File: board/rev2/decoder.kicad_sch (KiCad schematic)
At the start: 4 parts, among them U10 74VHC161

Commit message: 3.3V LDO
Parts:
- removed R22, R23: 33, Resistor_SMD:R_0402_1005Metric, symbol Device:R_Small_US
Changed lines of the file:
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@@
+	)
+	(junction
+		(at 173.99 76.2)
+		(diameter 0)
+		(color 0 0 0 0)
 	)
 	(junction
@@
 	)
 	(junction
-		(at 161.29 95.25)
-		(diameter 0)
-		(color 0 0 0 0)
-	)
-	(junction
 		(at 168.91 68.58)
 		(diameter 0)
@@
 		)
 	)
-	(wire
-		(pts
-			(xy 161.29 95.25) (xy 161.29 50.8)
-		)
-		(stroke
-			(width 0)
-			(type default)
-		)
-	)
 	(bus
 		(pts
@@
 	(wire
 		(pts
-			(xy 142.24 95.25) (xy 161.29 95.25)
+			(xy 142.24 76.2) (xy 173.99 76.2)
 		)
 		(stroke
@@
 	(wire
 		(pts
+			(xy 173.99 76.2) (xy 173.99 50.8)
+		)
+		(stroke
+			(width 0)
+			(type default)
+		)
+	)
+	(wire
+		(pts
 			(xy 123.19 71.12) (xy 125.73 71.12)
 		)
@@
 	(wire
 		(pts
-			(xy 161.29 50.8) (xy 171.45 50.8)
+			(xy 173.99 50.8) (xy 180.34 50.8)
 		)
 		(stroke
@@
 	(wire
 		(pts
+			(xy 173.99 76.2) (xy 173.99 106.68)
+		)
+		(stroke
+			(width 0)
+			(type default)
+		)
+	)
+	(wire
+		(pts
 			(xy 91.44 55.88) (xy 91.44 58.42)
 		)
@@
 	(wire
 		(pts
-			(xy 161.29 106.68) (xy 171.45 106.68)
+			(xy 173.99 106.68) (xy 180.34 106.68)
 		)
 		(stroke
@@
 	(wire
 		(pts
-			(xy 161.29 95.25) (xy 161.29 106.68)
-		)
-		(stroke
-			(width 0)
-			(type default)
-		)
-	)
-	(wire
-		(pts
 			(xy 44.45 48.26) (xy 67.31 48.26)
 		)
@@
 	(wire
 		(pts
-			(xy 176.53 50.8) (xy 180.34 50.8)
-		)
-		(stroke
-			(width 0)
-			(type default)
-		)
-	)
-	(wire
-		(pts
 			(xy 67.31 48.26) (xy 163.83 48.26)
 		)
@@
 		(pts
 			(xy 168.91 124.46) (xy 180.34 124.46)
-		)
-		(stroke
-			(width 0)
-			(type default)
-		)
-	)
-	(wire
-		(pts
-			(xy 176.53 106.68) (xy 180.34 106.68)
 		)
 		(stroke
@@
 	(hierarchical_label "RGB_CLK"
 		(shape input)
-		(at 142.24 95.25 180)
+		(at 142.24 76.2 180)
 		(effects
 			(font
@@
 	)
 	(symbol
-		(lib_id "Device:R_Small_US")
-		(at 173.99 50.8 90)
-		(unit 1)
-		(exclude_from_sim no)
-		(in_bom yes)
-		(on_board yes)
-		(dnp no)
-		(property "Reference" "R22"
-			(at 173.99 53.086 90)
-			(effects
-				(font
-					(size 1.27 1.27)
-				)
-			)
-		)
-		(property "Value" "33"
-			(at 173.99 55.118 90)
-			(effects
-				(font
-					(size 1.27 1.27)
-				)
-			)
-		)
-		(property "Footprint" "Resistor_SMD:R_0402_1005Metric"
-			(at 173.99 50.8 0)
-			(effects
-				(font
-					(size 1.27 1.27)
-				)
-				(hide yes)
-			)
-		)
-		(property "Datasheet" "~"
-			(at 173.99 50.8 0)
-			(effects
-				(font
-					(size 1.27 1.27)
-				)
-				(hide yes)
-			)
-		)
-		(property "Description" "Resistor, small US symbol"
-			(at 173.99 50.8 0)
-			(effects
-				(font
-					(size 1.27 1.27)
-				)
-				(hide yes)
-			)
-		)
-		(property "Part" "0402WGF330JTCE"
-			(at 173.99 50.8 90)
-			(effects
-				(font
-					(size 1.27 1.27)
-				)
-				(hide yes)
-			)
-		)
-		(property "LCSC" "C25105"
-			(at 173.99 50.8 90)
-			(effects
-				(font
-					(size 1.27 1.27)
-				)
-				(hide yes)
-			)
-		)
-		(pin "2"
-		)
-		(pin "1"
-		)
-		(instances
-			(project "mainboard"
-				(path "/32eb05c7-b4a6-42f3-8fb3-43453631100f/2c9586de-ca2f-4a0b-8ff8-8fdad1d1abcc"
-					(reference "R22")
-					(unit 1)
-				)
-			)
-		)
-	)
-	(symbol
 		(lib_id "Device:C_Small")
 		(at 99.06 58.42 90)
@@
 					(unit 1)
 				)
-			)
-		)
-	)
-	(symbol
-		(lib_id "Device:R_Small_US")
-		(at 173.99 106.68 90)
-		(unit 1)
-		(exclude_from_sim no)
-		(in_bom yes)
-		(on_board yes)
-		(dnp no)
-		(property "Reference" "R23"
-			(at 173.99 108.966 90)
-			(effects
-				(font
-					(size 1.27 1.27)
-				)
-			)
-		)
-		(property "Value" "33"
-			(at 173.99 110.998 90)
-			(effects
-				(font
-					(size 1.27 1.27)
-				)
-			)
-		)
-		(property "Footprint" "Resistor_SMD:R_0402_1005Metric"
-			(at 173.99 106.68 0)
-			(effects
-				(font
-					(size 1.27 1.27)
-				)
-				(hide yes)
-			)
-		)
-		(property "Datasheet" "~"
-			(at 173.99 106.68 0)
-			(effects
-				(font
-					(size 1.27 1.27)
-				)
-				(hide yes)
-			)
-		)
-		(property "Description" "Resistor, small US symbol"
-			(at 173.99 106.68 0)
-			(effects
-				(font
-					(size 1.27 1.27)
-				)
-				(hide yes)
-			)
-		)
-		(property "Part" "0402WGF330JTCE"
-			(at 173.99 106.68 90)
-			(effects
-				(font
-					(size 1.27 1.27)
-				)
-				(hide yes)
-			)
-		)
-		(property "LCSC" "C25105"
-			(at 173.99 106.68 90)
-			(effects
-				(font
-					(size 1.27 1.27)
-				)
-				(hide yes)
-			)
-		)
-		(pin "2"
-		)
-		(pin "1"
-		)
-		(instances
-			(project ""
-				(path "/32eb05c7-b4a6-42f3-8fb3-43453631100f/2c9586de-ca2f-4a0b-8ff8-8fdad1d1abcc"
-					(reference "R23")
-					(unit 1)
-				)

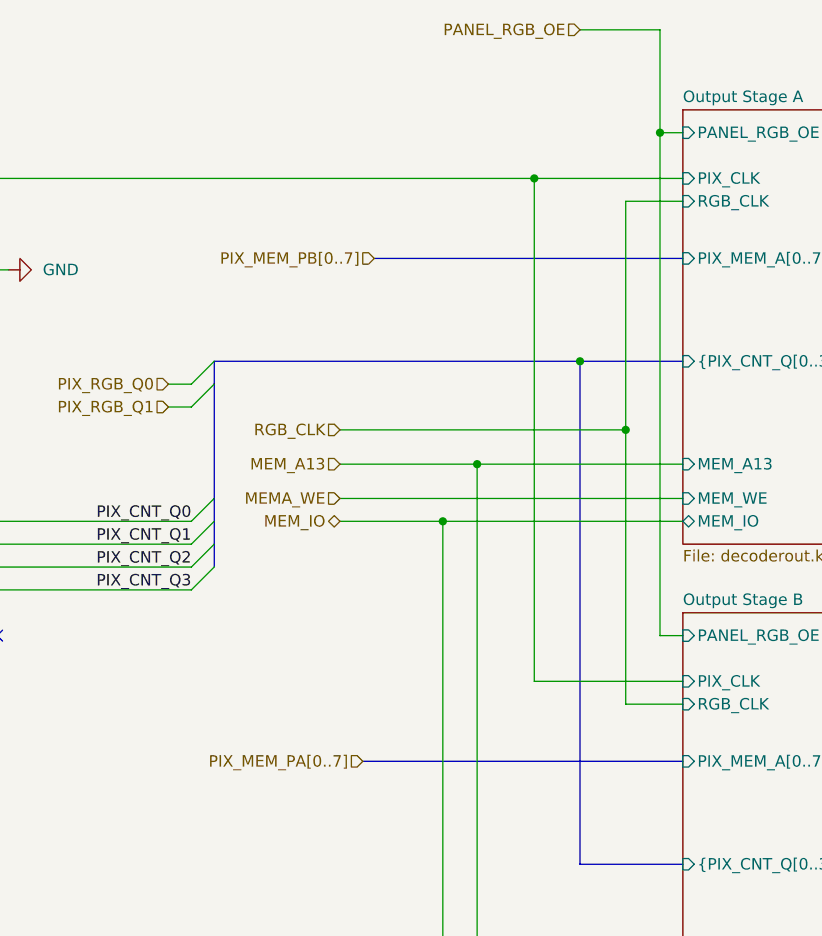
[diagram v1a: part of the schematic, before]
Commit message: Rough full board layout
also, start re-organizing which pins of buffers/gates are used for what

still need to reorder the mem i/o lines to align better

also fix duplicate pullups and fix mem_io isolation res
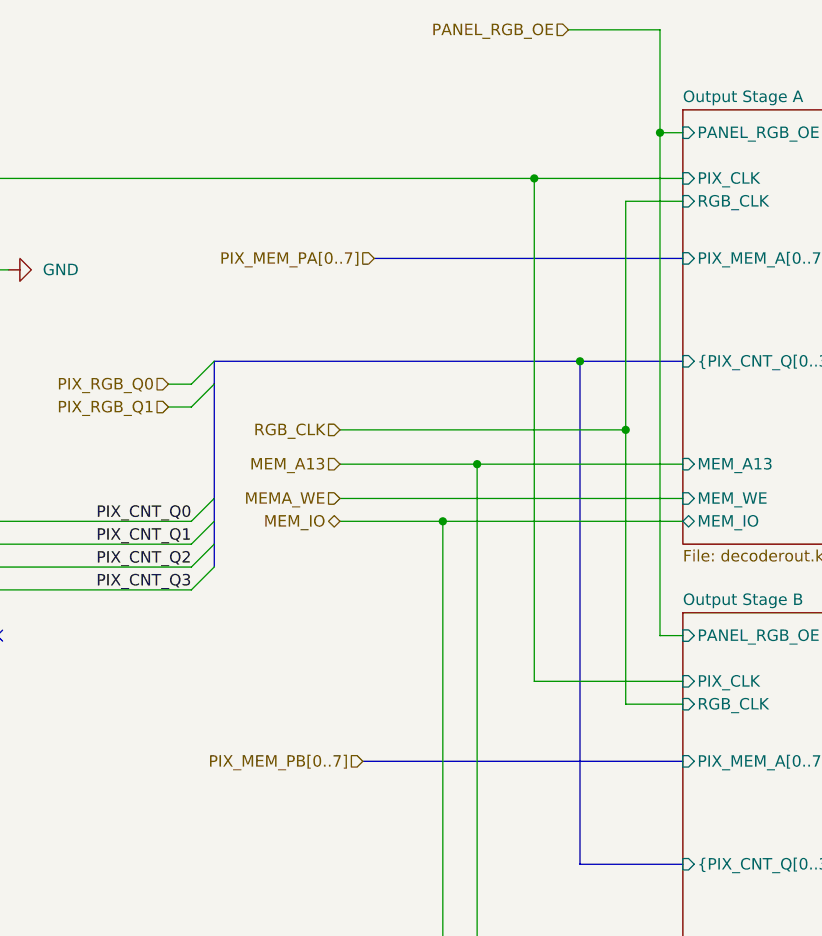
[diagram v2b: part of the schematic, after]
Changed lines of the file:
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@@
 	(wire
 		(pts
-			(xy 168.91 31.75) (xy 177.8 31.75)
+			(xy 167.64 31.75) (xy 177.8 31.75)
 		)
 		(stroke
@@
 		)
 	)
+	(hierarchical_label "PIX_MEM_PA[0..7]"
+		(shape input)
+		(at 146.05 57.15 180)
+		(effects
+			(font
+				(size 1.27 1.27)
+			)
+			(justify right)
+		)
+	)
 	(hierarchical_label "PIX_CNT_PE"
 		(shape input)
@@
 		)
 	)
+	(hierarchical_label "MEM_A13"
+		(shape input)
+		(at 142.24 80.01 180)
+		(effects
+			(font
+				(size 1.27 1.27)
+			)
+			(justify right)
+		)
+	)
 	(hierarchical_label "PIX_MEM_PB[0..7]"
 		(shape input)
-		(at 146.05 57.15 180)
-		(effects
-			(font
-				(size 1.27 1.27)
-			)
-			(justify right)
-		)
-	)
-	(hierarchical_label "MEM_A13"
-		(shape input)
-		(at 142.24 80.01 180)
+		(at 144.78 113.03 180)
 		(effects
 			(font
@@
 		(shape input)
 		(at 44.45 48.26 180)
-		(effects
-			(font
-				(size 1.27 1.27)
-			)
-			(justify right)
-		)
-	)
-	(hierarchical_label "PIX_MEM_PA[0..7]"
-		(shape input)
-		(at 144.78 113.03 180)
 		(effects
 			(font
@@
 	(hierarchical_label "PANEL_RGB_OE"
 		(shape input)
-		(at 168.91 31.75 180)
-		(effects
-			(font
+		(at 167.64 31.75 180)
+		(effects
+			(font
